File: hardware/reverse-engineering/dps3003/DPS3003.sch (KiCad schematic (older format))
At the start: 54 parts, among them U2 SGM8582

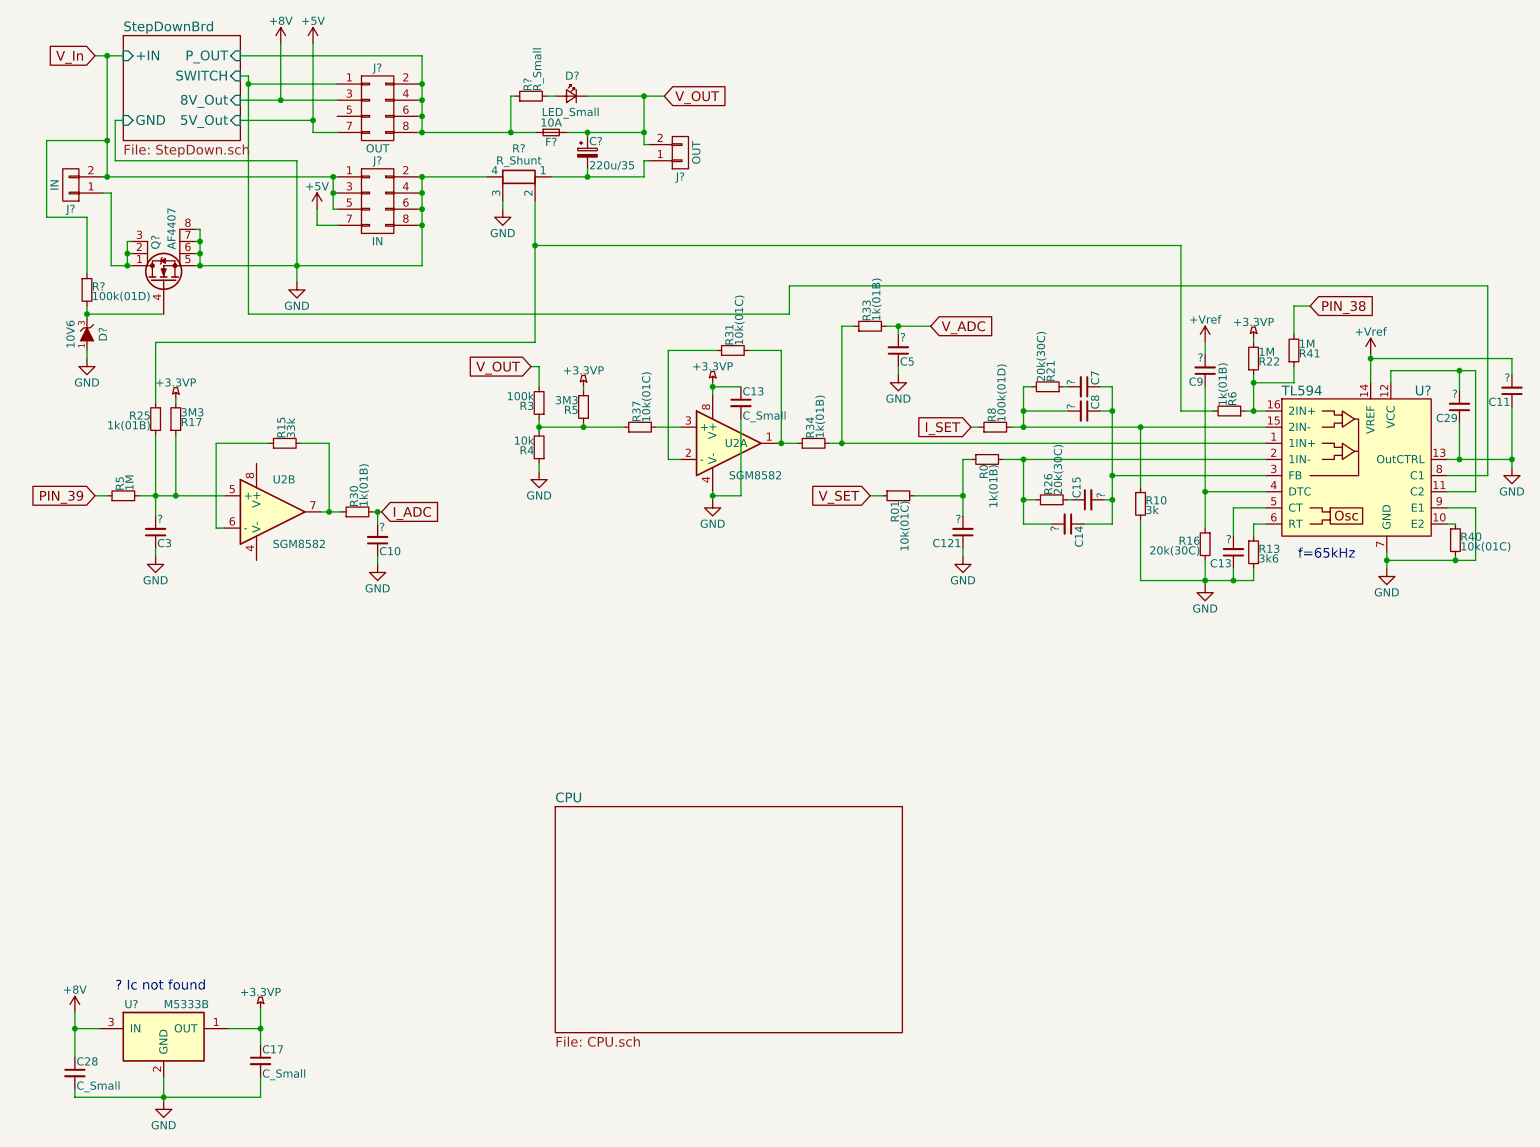
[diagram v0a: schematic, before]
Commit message: Fixed #61
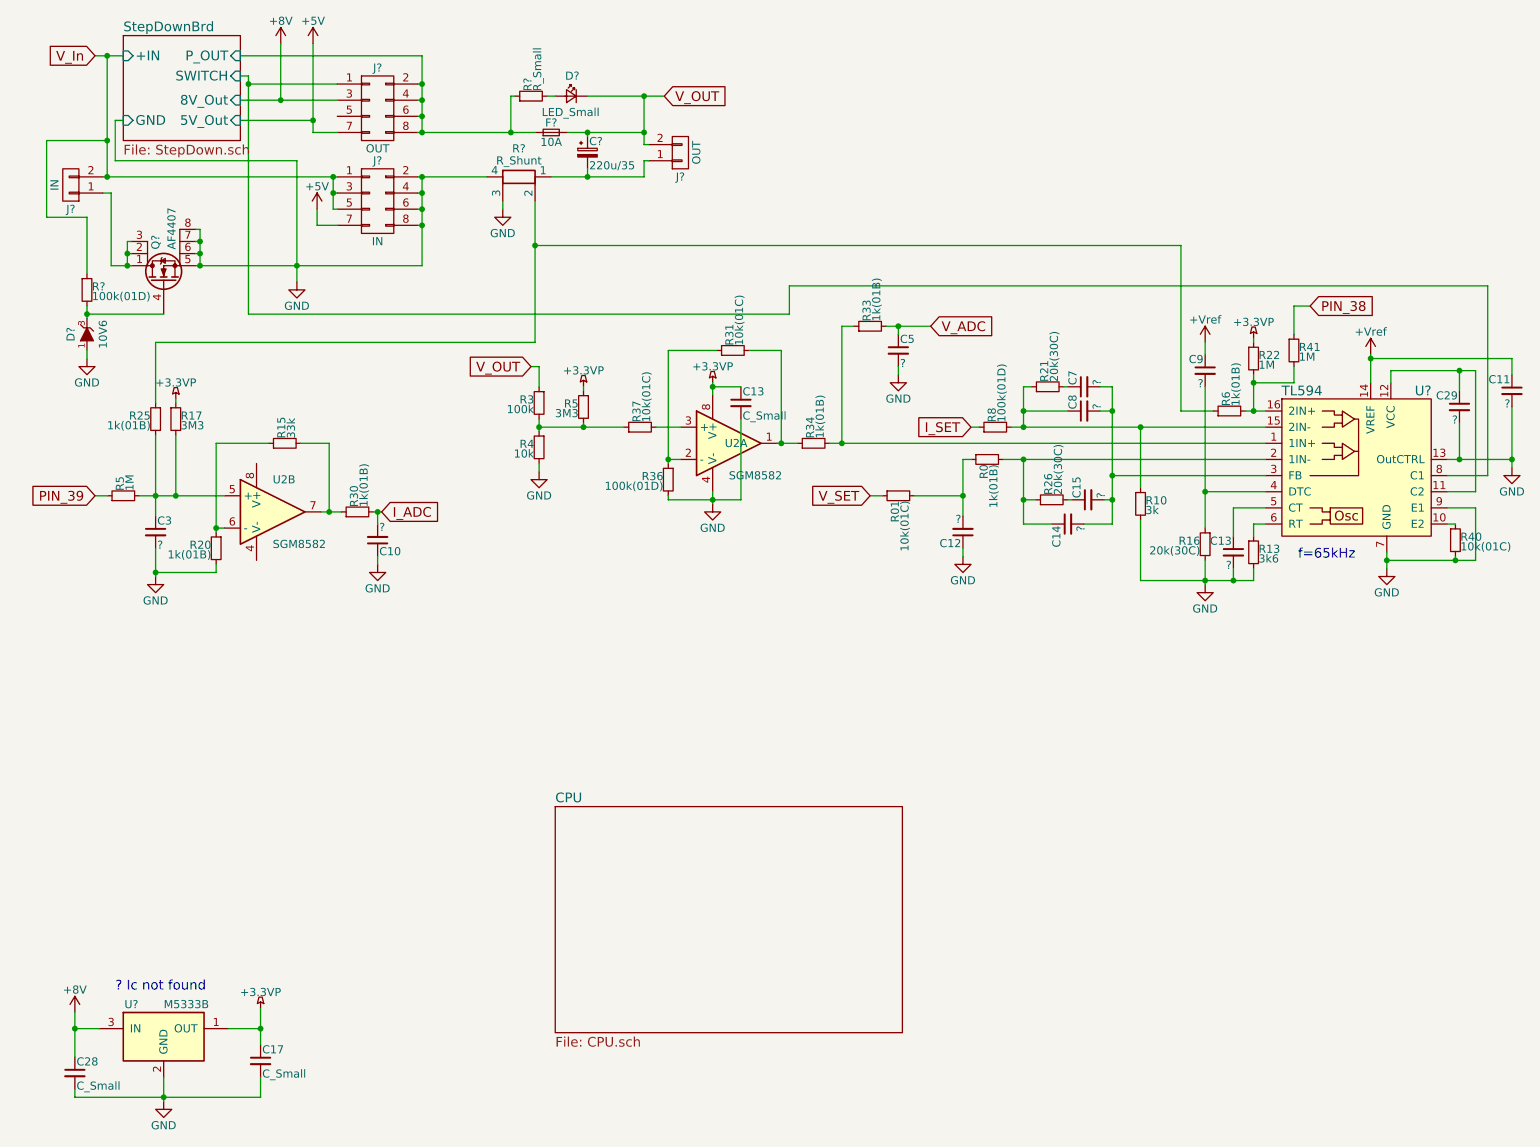
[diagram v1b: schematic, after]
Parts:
- added R20: 1k(01B), symbol R_Small
- added R36: 100k(01D), symbol R_Small
- renumbered C121 to C12
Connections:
- net +3.3VP: now also R17.1, R22.1, R5.1; no longer R17.2, R22.2, R5.2
- net +Vref: now also C11.1, C9.1; no longer C11.2, C9.2
- net GND: now also C11.2, C13.2, C29.2, C3.2, C5.2, R4.2, R20.2, R36.2; no longer C11.1, C13.1, C29.1, C3.1, C5.1, R4.1
- net PIN_38: now also R41.1; no longer R41.2
- net V_ADC: now also C5.1; no longer C5.2
- net V_OUT: now also R3.1; no longer R3.2
- net at R31.1, U2.2 (-): now also R36.1
- net at R25.2, R5.2, U2.5 (+): now also C3.1, R17.2; no longer C3.2, R17.1
- net at R15.1, U2.6 (-): now also R20.1
- net at U?.11 (C2), U?.12 (VCC): now also C29.1; no longer C29.2
- net at R10.1, R8.2, U?.15 (2IN-): now also C8.1, R21.1; no longer C8.2, R21.2
- net at R0.2, R26.1, U?.2 (1IN-): now also C14.1; no longer C14.2
- net at R16.1, U?.4 (DTC): now also C9.2; no longer C9.1
- net at U?.5 (CT): now also C13.1; no longer C13.2
- net at R25.1, R?.2: now also R6.1; no longer R6.2
- net at C7.2: now also C14.2, C15.2, C8.2, U?.3 (FB); no longer R21.1
- new net: R22.2, R41.2, R6.2, U?.16 (2IN+)
- new net: R3.2, R37.1, R4.1, R5.2
- new net: C7.1, R21.2
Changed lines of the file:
@@
 LIBS:my_sensors
 LIBS:my_transistors
-LIBS:DPS3203-cache
+LIBS:DPS3003-cache
 EELAYER 25 0
 EELAYER END
@@
 Sheet 1 3
 Title ""
-Date ""
-Rev ""
+Date "2017-11-16"
+Rev "v0.2"
 Comp ""
-Comment1 ""
+Comment1 "v0.2: Optical Changes, Renamed, R36, R20 added"
 Comment2 ""
 Comment3 ""
@@
 F 3 "" H 3750 1225 50  0001 C CNN
 	1    3750 1225
-	1    0    0    -1
+	1    0    0    1
 $EndComp
 Connection ~ 3975 1225
@@
 	4775 2575 4475 2575
 Wire Wire Line
-	4475 2575 4475 3250
+	4475 2575 4475 3275
 Wire Wire Line
 	4475 3250 4550 3250
@@
 L GND #PWR?
 U 1 1 5969443D
-P 4750 3500
-F 0 "#PWR?" H 4750 3250 50  0001 C CNN
-F 1 "GND" H 4750 3350 50  0000 C CNN
-F 2 "" H 4750 3500 50  0001 C CNN
-F 3 "" H 4750 3500 50  0001 C CNN
-	1    4750 3500
-	1    0    0    -1
-$EndComp
-Wire Wire Line
-	4750 3450 4750 3500
+P 4750 3525
+F 0 "#PWR?" H 4750 3275 50  0001 C CNN
+F 1 "GND" H 4750 3375 50  0000 C CNN
+F 2 "" H 4750 3525 50  0001 C CNN
+F 3 "" H 4750 3525 50  0001 C CNN
+	1    4750 3525
+	1    0    0    -1
+$EndComp
+Wire Wire Line
+	4750 3450 4750 3525
 Wire Wire Line
 	4750 2775 4750 2850
@@
 Connection ~ 4750 2800
 Wire Wire Line
-	4750 3475 4925 3475
-Wire Wire Line
-	4925 3475 4925 3000
-Connection ~ 4750 3475
+	4475 3500 4925 3500
+Wire Wire Line
+	4925 3500 4925 3000
+Connection ~ 4750 3500
 $Sheet
 S 3775 5400 2150 1400
@@
 F 3 "" H 6950 3650 50  0001 C CNN
 	1    6950 3650
-	0    1    1    0
+	0    -1   1    0
 $EndComp
 Wire Wire Line
@@
 F 3 "" H 7975 3825 50  0001 C CNN
 	1    7975 3825
-	-1   0    0    1
+	-1   0    0    -1
 $EndComp
 Wire Wire Line
@@
 Connection ~ 6675 3250
 $Comp
-L C_Small C121
+L C_Small C12
 U 1 1 596A3BFB
 P 6300 3700
-F 0 "C121" H 6310 3770 50  0000 L CNN
+F 0 "C12" H 6310 3770 50  0000 L CNN
 F 1 "?" H 6310 3620 50  0000 L CNN
 F 2 "" H 6300 3700 50  0001 C CNN
@@
 F 3 "" H 9375 2925 50  0001 C CNN
 	1    9375 2925
-	-1   0    0    1
+	-1   0    0    -1
 $EndComp
 Wire Wire Line
@@
 F 3 "" H 9700 2825 50  0001 C CNN
 	1    9700 2825
-	-1   0    0    1
+	-1   0    0    -1
 $EndComp
 Wire Wire Line
@@
 F 3 "" H 7800 2700 50  0001 C CNN
 	1    7800 2700
-	-1   0    0    1
+	-1   0    0    -1
 $EndComp
 $Comp
@@
 F 3 "" H 7950 2950 50  0001 C CNN
 	1    7950 2950
-	0    1    -1   0
+	0    -1   -1   0
 $EndComp
 Wire Wire Line
@@
 F 3 "" H 7050 2800 50  0001 C CNN
 	1    7050 2800
-	0    1    -1   0
+	0    -1   -1   0
 $EndComp
 $Comp
@@
 F 3 "" H 7050 2950 50  0001 C CNN
 	1    7050 2950
-	0    1    -1   0
+	0    -1   -1   0
 $EndComp
 Wire Wire Line
@@
 F 3 "" H 6825 2800 50  0001 C CNN
 	1    6825 2800
-	0    1    -1   0
+	0    -1   -1   0
 $EndComp
 Wire Wire Line
@@
 F 3 "" H 3675 2900 50  0001 C CNN
 	1    3675 2900
-	-1   0    0    1
+	-1   0    0    -1
 $EndComp
 $Comp
@@
 F 3 "" H 3675 3175 50  0001 C CNN
 	1    3675 3175
-	-1   0    0    1
+	-1   0    0    -1
 $EndComp
 $Comp
@@
 F 3 "" H 3950 2925 50  0001 C CNN
 	1    3950 2925
-	-1   0    0    1
+	-1   0    0    -1
 $EndComp
 Wire Wire Line
@@
 F 3 "" H 8100 2625 50  0001 C CNN
 	1    8100 2625
-	1    0    0    1
+	1    0    0    -1
 $EndComp
 $Comp
@@
 F 3 "" H 1300 3700 50  0001 C CNN
 	1    1300 3700
-	1    0    0    1
+	1    0    0    -1
 $EndComp
 $Comp
@@
 F 3 "" H 1425 3000 50  0001 C CNN
 	1    1425 3000
-	1    0    0    1
+	1    0    0    -1
 $EndComp
 $Comp
@@
 	2000 3150 1675 3150
 Wire Wire Line
-	1675 3150 1675 3675
+	1675 3150 1675 3700
 Wire Wire Line
 	1675 3675 1725 3675
@@
 L GND #PWR?
 U 1 1 596B46D3
-P 1300 3850
-F 0 "#PWR?" H 1300 3600 50  0001 C CNN
-F 1 "GND" H 1300 3700 50  0000 C CNN
-F 2 "" H 1300 3850 50  0001 C CNN
-F 3 "" H 1300 3850 50  0001 C CNN
-	1    1300 3850
-	1    0    0    -1
-$EndComp
-Wire Wire Line
-	1300 3800 1300 3850
+P 1300 3975
+F 0 "#PWR?" H 1300 3725 50  0001 C CNN
+F 1 "GND" H 1300 3825 50  0000 C CNN
+F 2 "" H 1300 3975 50  0001 C CNN
+F 3 "" H 1300 3975 50  0001 C CNN
+	1    1300 3975
+	1    0    0    -1
+$EndComp
+Wire Wire Line
+	1300 3800 1300 3975
 $Comp
 L C_Small C5
@@
 F 3 "" H 5900 2575 50  0001 C CNN
 	1    5900 2575
-	1    0    0    1
+	1    0    0    -1
 $EndComp
 $Comp
@@
 F 3 "" H 875 2475 50  0000 C CNN
 	1    875  2475
-	0    1    1    0
+	0    -1   1    0
 $EndComp
 Connection ~ 875  2350
@@
 F 3 "" H 8350 2575 50  0001 C CNN
 	1    8350 2575
-	1    0    0    1
+	1    0    0    -1
 $EndComp
 Wire Wire Line
@@
 Wire Wire Line
 	8350 2300 8350 2475
+$Comp
+L R_Small R36
+U 1 1 5A0D72CF
+P 4475 3375
+F 0 "R36" H 4505 3395 50  0000 L CNN
+F 1 "100k(01D)" H 4505 3335 50  0000 L CNN
+F 2 "" H 4475 3375 50  0001 C CNN
+F 3 "" H 4475 3375 50  0001 C CNN
+	1    4475 3375
+	-1   0    0    -1
+$EndComp
+Connection ~ 4475 3250
+Wire Wire Line
+	4475 3475 4475 3500
+$Comp
+L R_Small R20
+U 1 1 5A0D88C2
+P 1675 3800
+F 0 "R20" H 1705 3820 50  0000 L CNN
+F 1 "1k(01B)" H 1705 3760 50  0000 L CNN
+F 2 "" H 1675 3800 50  0001 C CNN
+F 3 "" H 1675 3800 50  0001 C CNN
+	1    1675 3800
+	-1   0    0    -1
+$EndComp
+Connection ~ 1675 3675
+Wire Wire Line
+	1675 3900 1675 3950
+Wire Wire Line
+	1675 3950 1300 3950
+Connection ~ 1300 3950
 $EndSCHEMATC
